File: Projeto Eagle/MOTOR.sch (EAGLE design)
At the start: 9 parts, among them IC1 BCP56, J1 CONECTOR_MACHO, J2 CONECTOR_FEMEA, U1 74HC132

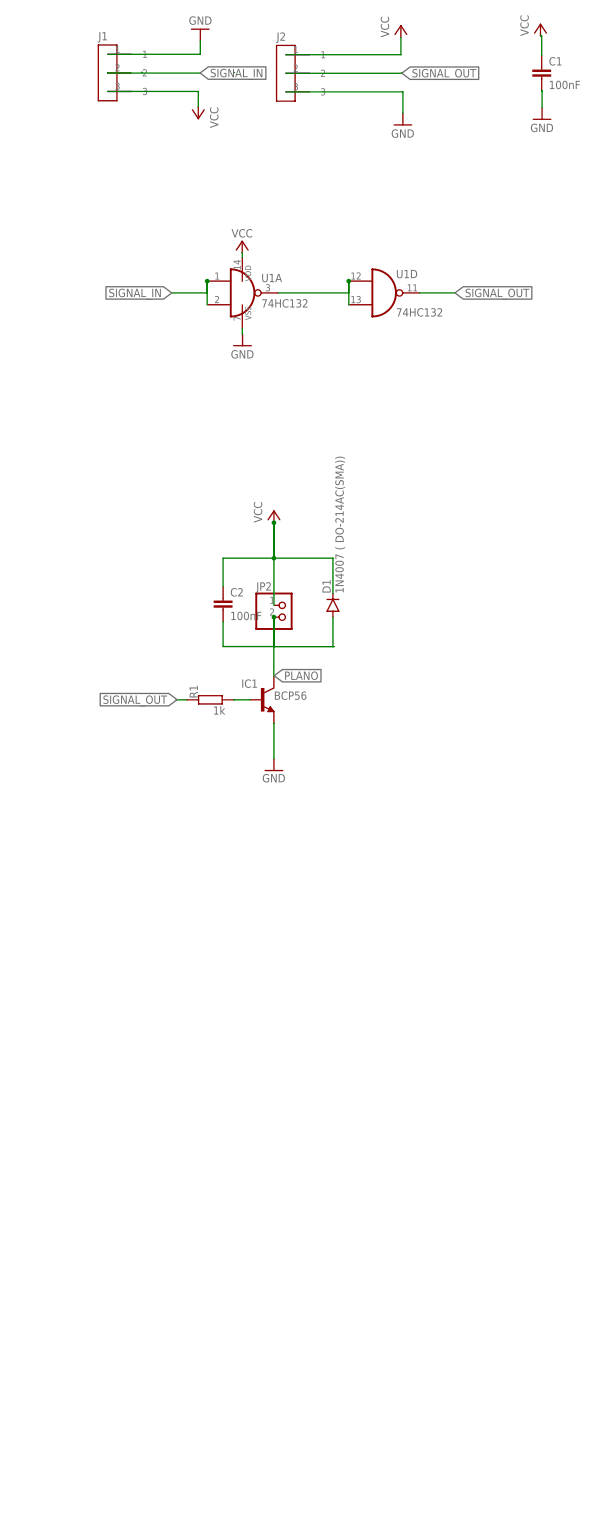
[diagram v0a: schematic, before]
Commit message: correção de pads, adição de label para versionamento e plano de VCC
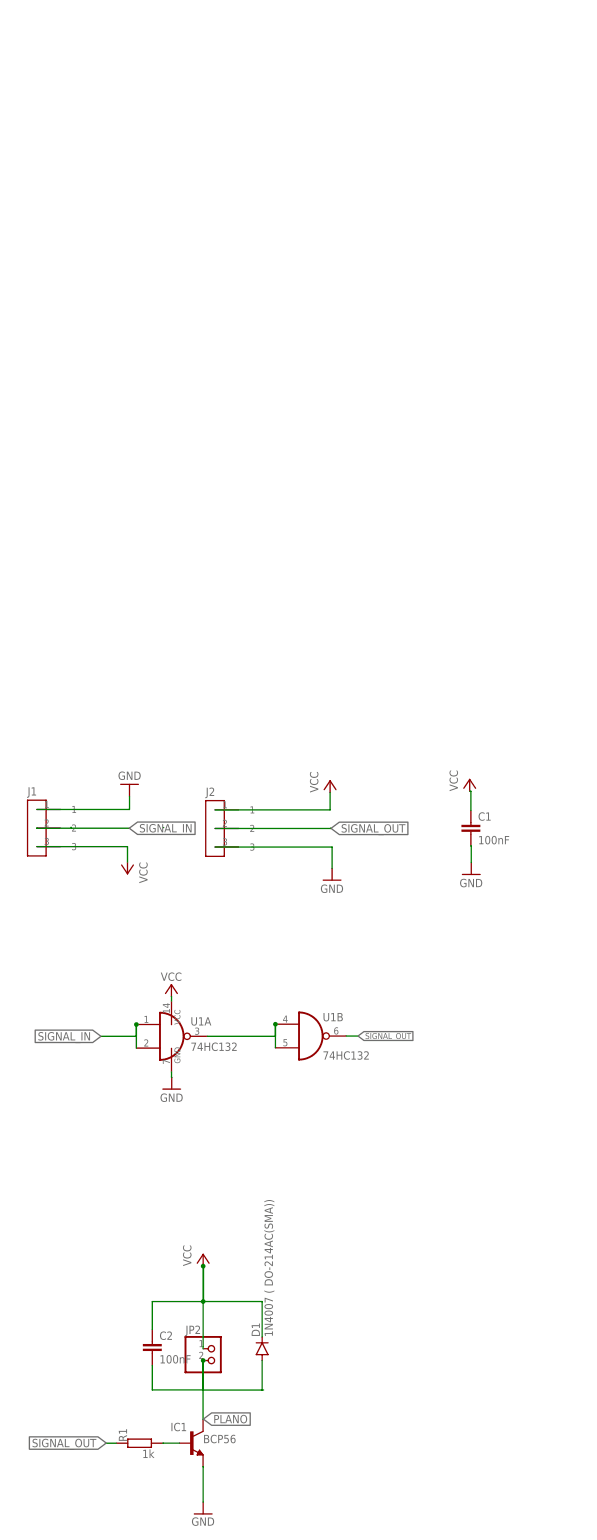
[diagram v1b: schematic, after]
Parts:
- U1: device 40xx:4011D -> 74xx-eu:74HC00D
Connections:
- removed net N$1: U1A.O, U1D.I0, U1D.I1
- new net N$3: U1A.O, U1B.I0, U1B.I1
- net GND: now also U1P.GND; no longer U1P.VSS
- net SIGNAL_OUT: now also U1B.O; no longer U1D.O
- net VCC: now also U1P.VCC; no longer U1P.VDD
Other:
- moved on the sheet: C1, C2, D1, IC1, J1, J2, JP2, R1, U1A
